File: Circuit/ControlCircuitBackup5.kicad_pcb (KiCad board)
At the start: 2 copper layers, 120 x 120 mm, 123 parts, among them CON501 AVR-ISP-10, IC501 ATMEGA644-A, K201 Meisei-m4-24h, K202 Meisei-m4-24h, K203 Meisei-m4-24h, K204 Meisei-m4-24h, K205 Meisei-m4-24h, K206 Meisei-m4-24h, K207 Meisei-m4-24h, K208 Meisei-m4-24h, P101 CONN_01X08, P102 CONN_01X08, P103 CONN_01X08, P104 CONN_01X08, P105 CONN_01X08, P106 CONN_01X08, P107 CONN_01X02, Q201 Q_NPN_BCE, Q202 Q_NPN_BCE, Q203 Q_NPN_BCE, Q204 Q_NPN_BCE, Q205 Q_NPN_BCE, Q206 Q_NPN_BCE, Q207 Q_NPN_BCE, Q208 Q_NPN_BCE, U301 LTV-817, U302 LTV-817, U303 LTV-817, U304 LTV-817, U305 LTV-817, U306 LTV-817, U307 LTV-817, U308 LTV-817, Y501 Crystal

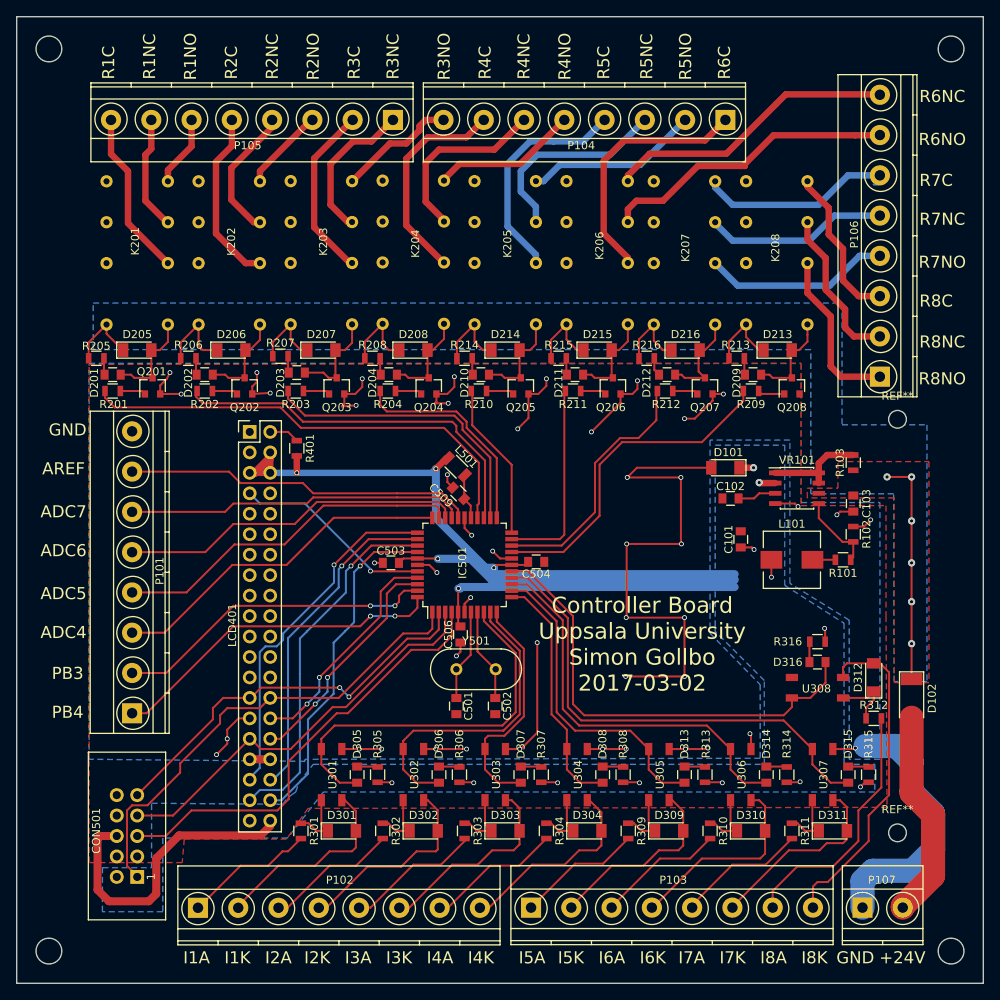
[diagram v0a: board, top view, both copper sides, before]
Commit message: PCB rev 1 ordered. Components counted
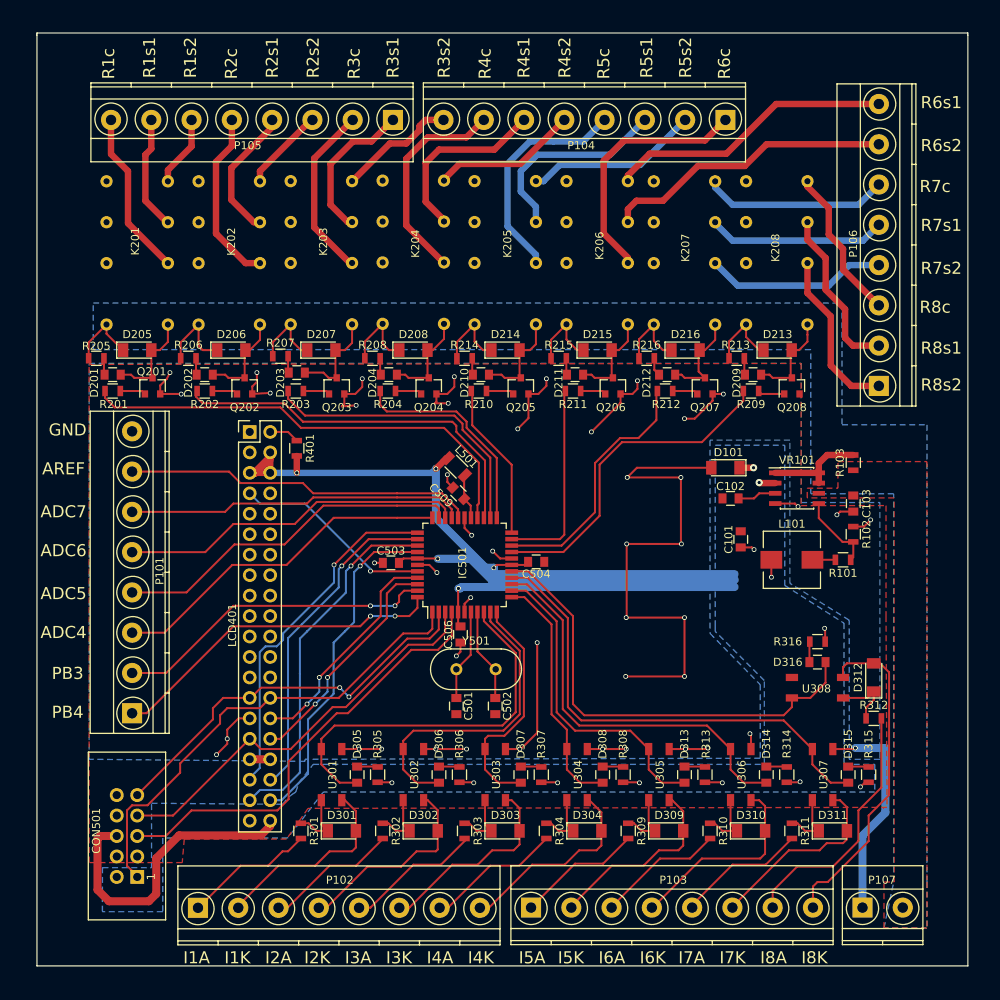
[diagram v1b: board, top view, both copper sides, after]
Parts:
- removed D102: D, Diodes_SMD:D_MELF_Standard
- removed REF** (x4): MountingHole_3.2mm_M3_ISO14580, Mounting_Holes:MountingHole_3.2mm_M3_ISO14580
- removed REF** (x2): MountingHole_2.2mm_M2_ISO14580, Mounting_Holes:MountingHole_2.2mm_M2_ISO14580
- moved P106 1.15 mm to (153.0, 76.8)
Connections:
- P107 pad 2: Net-(D102-Pad2) -> +24V
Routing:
- net +24V: track 105.7 -> 77.4 mm, vias 6 -> 0
- net Net-(D102-Pad2): track 26.3 -> 0.00 mm
- net GND: track 256.2 -> 248.6 mm
- net /RelayOutputs/OR8sel1: track 20.2 -> 21.3 mm
- net /OR6s1: track 37.5 -> 36.8 mm
- net /OR6s2: track 36.7 -> 36.1 mm
- net /OR7c: track 23.4 -> 22.8 mm
- net /RelayOutputs/OR7sel1: track 22.9 -> 22.3 mm
- net /OR7s2: track 24.3 -> 23.7 mm
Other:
- board size 120 x 120 mm -> 115.6 x 115.8 mm
- rule pad_to_mask_clearance: 0.05 -> 0.2
- board text added: "R1c"
- board text added: "R1s1"
- board text added: "R1s2"
- board text added: "R2c"
- board text added: "R2s1"
- board text added: "R2s2"
- board text added: "R3c"
- board text added: "R3s1"
- board text added: "R3s2"
- board text added: "R4c"
- board text added: "R4s1"
- board text added: "R4s2"
- board text added: "R5c"
- board text added: "R5s1"
- board text added: "R5s2"
- board text added: "R6c"
- board text added: "R6s1"
- board text added: "R6s2"
- board text added: "R7c"
- board text added: "R7s1"
- board text added: "R7s2"
- board text added: "R8c"
- board text added: "R8s1"
- board text added: "R8s2"
- board text removed: "+24V"
- board text removed: "Controller Board Uppsala University Simon Gollbo 2017-03-02"
- board text removed: "R1C"
- board text removed: "R1NC"
- board text removed: "R1NO"
- board text removed: "R2C"
- board text removed: "R2NC"
- board text removed: "R2NO"
- board text removed: "R3C"
- board text removed: "R3NC"
- board text removed: "R3NO"
- board text removed: "R4C"
- board text removed: "R4NC"
- board text removed: "R4NO"
- board text removed: "R5C"
- board text removed: "R5NC"
- board text removed: "R5NO"
- board text removed: "R6C"
- board text removed: "R6NC"
- board text removed: "R6NO"
- board text removed: "R7C"
- board text removed: "R7NC"
- board text removed: "R7NO"
- board text removed: "R8C"
- board text removed: "R8NC"
- board text removed: "R8NO"
